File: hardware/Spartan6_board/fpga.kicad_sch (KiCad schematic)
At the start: 19 parts, among them J2 Conn_02x05_Odd_Even, J8 JTAG, U5 XC6SLX16-FTG256, Y1 33MHz

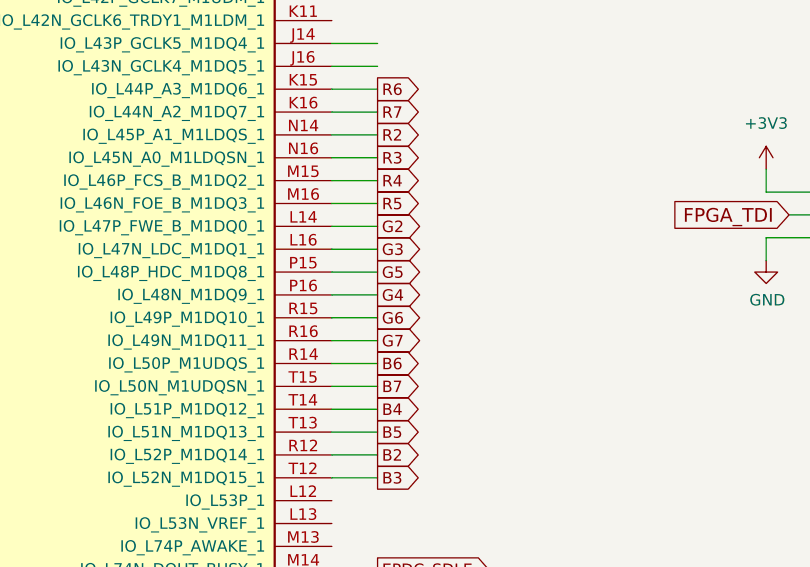
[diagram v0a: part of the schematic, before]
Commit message: fixed mixup of pins G5/G4 (3rd diff pair ODD) and DE/PCLK (3rd diff pair EVEN), now with correct polarity for diff pairs
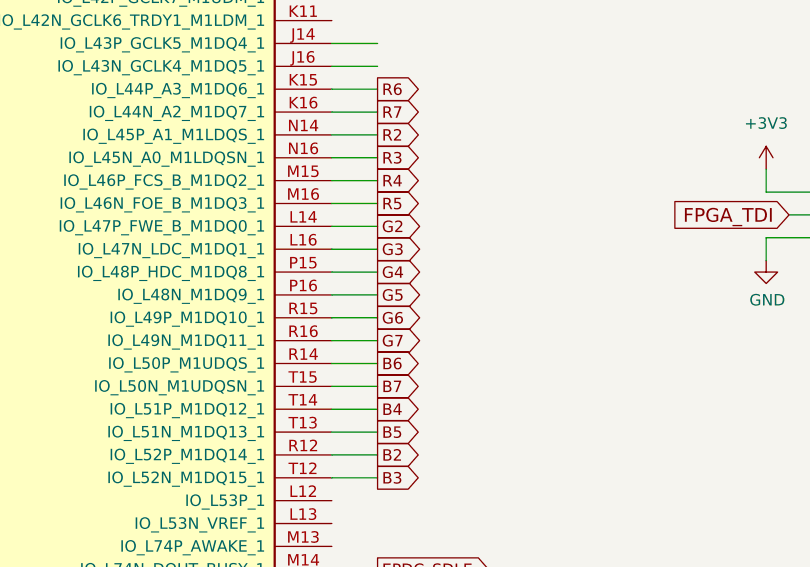
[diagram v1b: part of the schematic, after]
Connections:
- net G4: now also U5.P15 (IO_L48P_HDC_M1DQ8_1); no longer U5.P16 (IO_L48N_M1DQ9_1)
- net G5: now also U5.P16 (IO_L48N_M1DQ9_1); no longer U5.P15 (IO_L48P_HDC_M1DQ8_1)

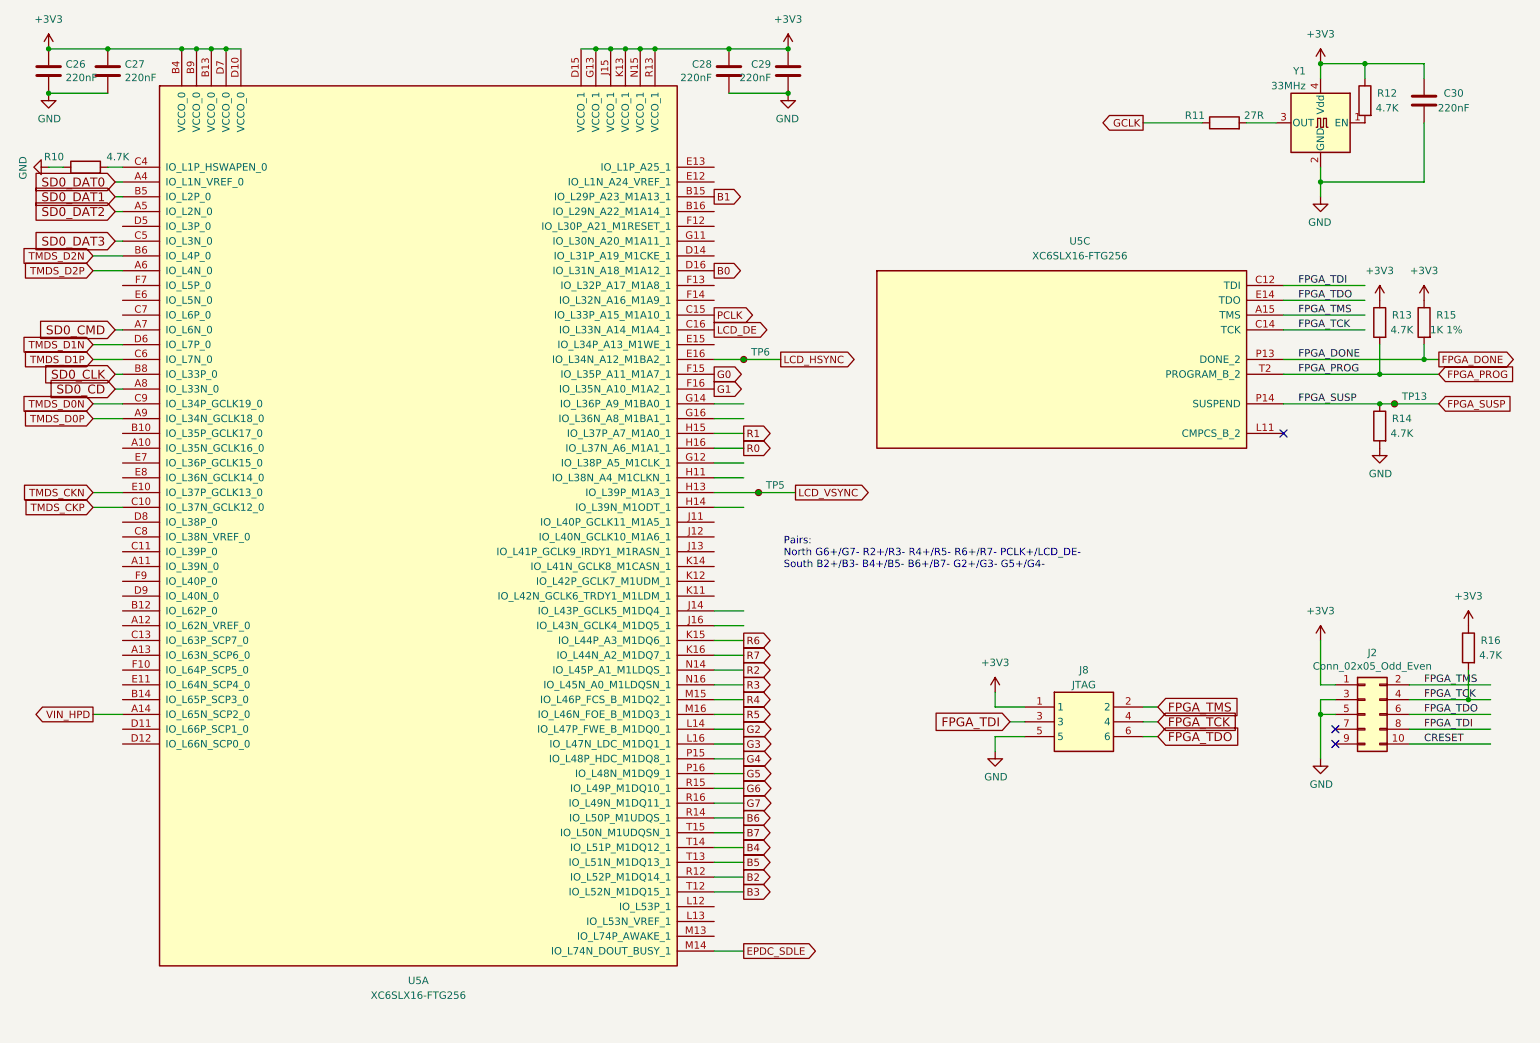
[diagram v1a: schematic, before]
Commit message: change DVI FPC pinout to match DVI connector (G-S-S-G), and FPGA device from XC6SLX16-FTG256 to XC6SLX25-3FTG256C
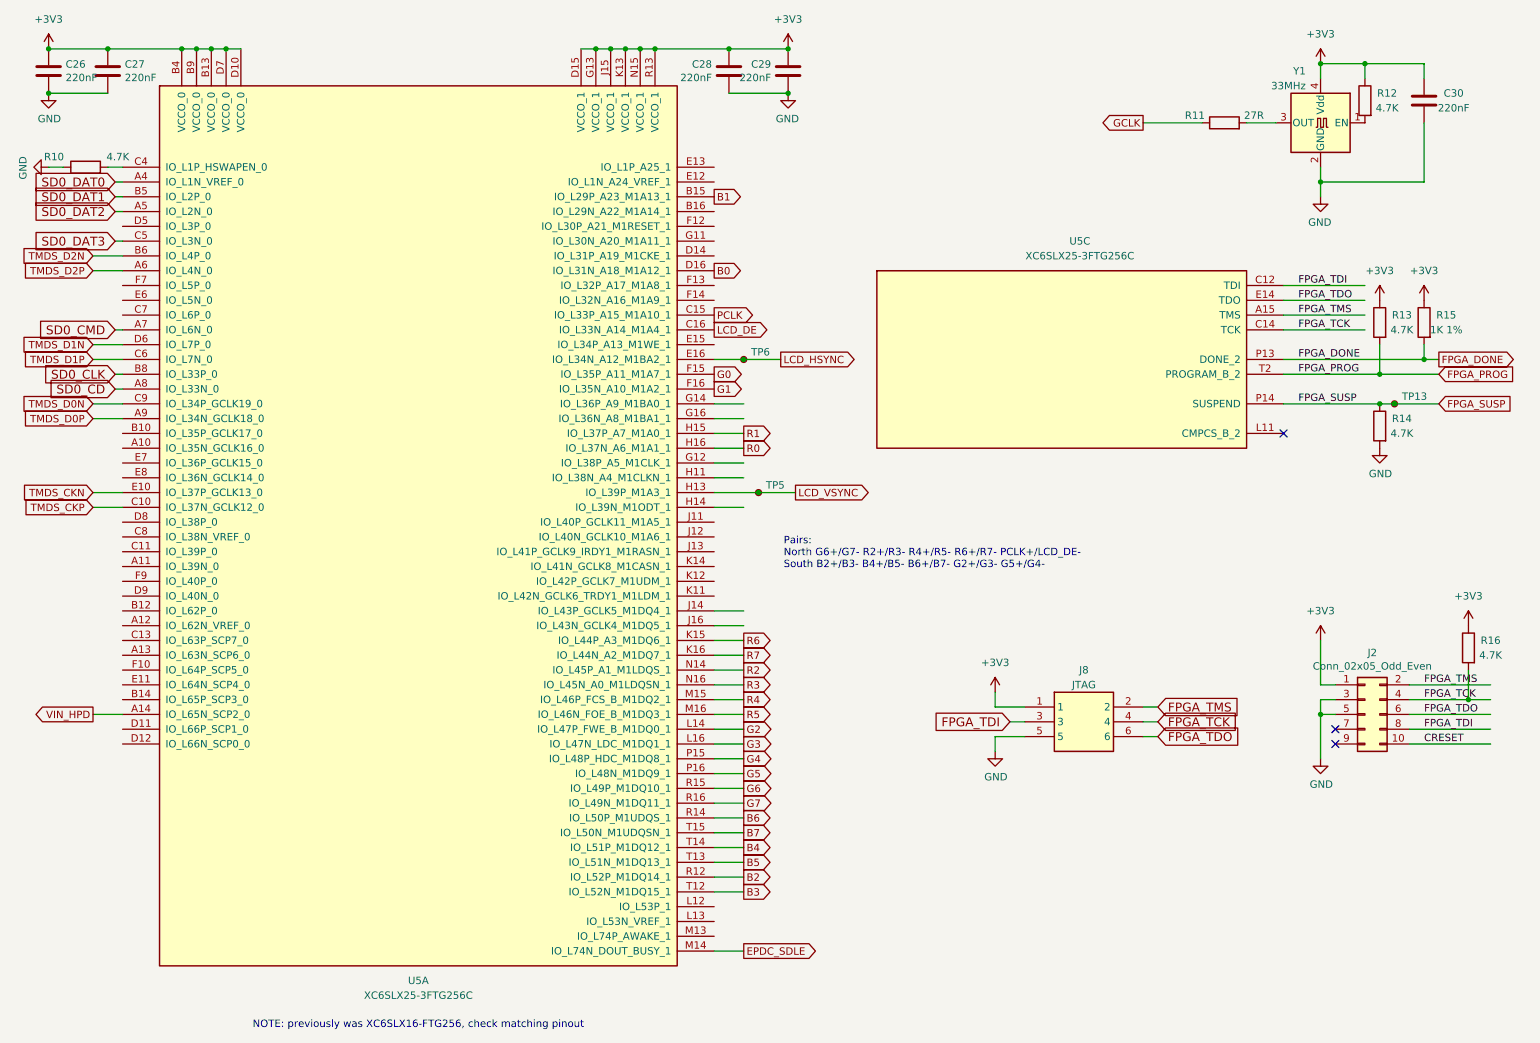
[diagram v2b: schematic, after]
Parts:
- U5: value XC6SLX16-FTG256 -> XC6SLX25-3FTG256C; LCSC Part Number C39313 -> C1521716
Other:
- note added: "NOTE: previously was XC6SLX16-FTG256, check matching pinout"
- title: Caster EPDC -> Spartan 6 FPGA board
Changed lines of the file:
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@@
 	(paper "A4")
 	(title_block
-		(title "Caster EPDC")
-		(date "2022-07-03")
-		(rev "R0.4")
+		(title "Spartan 6 FPGA board")
+		(date "2026-09-17")
+		(rev "R0.1")
 		(company "Copyright 2022 Modos / Engineer: Wenting Zhang")
 	)
@@
 		)
 	)
+	(text "NOTE: previously was XC6SLX16-FTG256, check matching pinout"
+		(exclude_from_sim no)
+		(at 91.44 193.04 0)
+		(effects
+			(font
+				(size 1.27 1.27)
+			)
+		)
+	)
 	(label "FPGA_TMS"
 		(at 242.57 71.12 0)
@@
 			)
 		)
-		(property "Value" "XC6SLX16-FTG256"
+		(property "Value" "XC6SLX25-3FTG256C"
 			(at 91.44 187.96 0)
 			(effects
@@
 			)
 		)
-		(property "LCSC Part Number" "C39313"
+		(property "LCSC Part Number" "C1521716"
 			(at 91.44 104.14 0)
 			(effects
@@
 			)
 		)
-		(property "Value" "XC6SLX16-FTG256"
+		(property "Value" "XC6SLX25-3FTG256C"
 			(at 205.0415 60.96 0)
 			(effects
@@
 			)
 		)
-		(property "LCSC Part Number" "C39313"
+		(property "LCSC Part Number" "C1521716"
 			(at 201.93 78.74 0)
 			(effects

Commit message: review and update manufacturing constraints (via size, etc.)
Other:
- company: Copyright 2022 Modos / Engineer: Wenting Zhang -> (C) 2025-2026 Victor Suarez Rovere <suarezvictor@gmail.com>
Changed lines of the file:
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@@
 	(title_block
 		(title "Spartan 6 FPGA board")
-		(date "2026-09-17")
+		(date "2026-09-18")
 		(rev "R0.1")
-		(company "Copyright 2022 Modos / Engineer: Wenting Zhang")
+		(company "(C) 2025-2026 Victor Suarez Rovere <suarezvictor@gmail.com>")
+		(comment 1 "Copyright 2023 Modos / Engineer: Wenting Zhang")
 	)
 	(junction

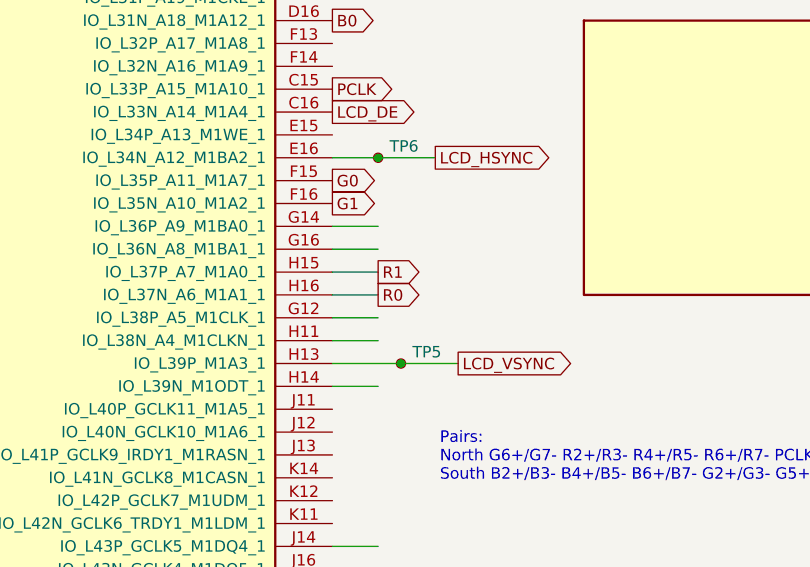
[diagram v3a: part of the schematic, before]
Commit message: fix R0/R1 mixup
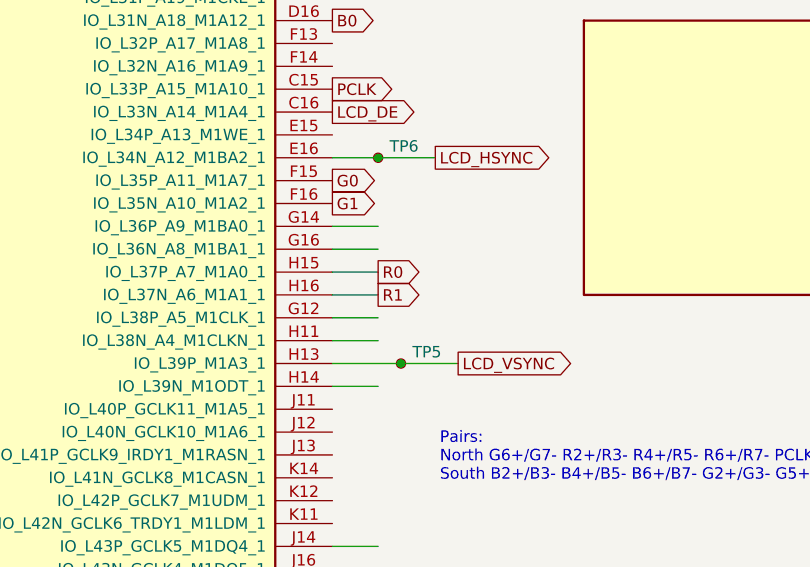
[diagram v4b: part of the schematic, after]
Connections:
- net R0: now also U5.H15 (IO_L37P_A7_M1A0_1); no longer U5.H16 (IO_L37N_A6_M1A1_1)
- net R1: now also U5.H16 (IO_L37N_A6_M1A1_1); no longer U5.H15 (IO_L37P_A7_M1A0_1)
